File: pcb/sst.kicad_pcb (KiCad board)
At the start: 2 copper layers, 80 x 85 mm, 36 parts, among them X1 CONN_INPUTS, X2 CONN_PWR, X3 CONN_SPI, X4 CONN_I2C, X5 CONN_INPUTS

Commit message: [2024-12-24 15:48] coursework for this day
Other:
- board size 80 x 85 mm -> 80 x 84.8 mm
- board text added: "0"
- board text added: "0 mm"
- board text added: "0,0000 mm / 0,0000 mm"
- board text added: "0,01 mm"
- board text added: "0,02"
- board text added: "0,035 mm"
- board text added: "0,3000 mm"
- board text added: "1"
- board text added: "1,51 mm"
- board text added: "1,6000 mm"
- board text added: "2"
- board text added: "3,3"
- board text added: "4,5"
- board text added: "80,0000 mm x 84,7500 mm"
- board text added: "B.Cu"
- board text added: "B.Mask"
- board text added: "B.Paste"
- board text added: "B.Silkscreen"
- board text added: "Bottom Silk Screen"
- board text added: "Bottom Solder Mask"
- board text added: "Bottom Solder Paste"
- board text added: "F.Cu"
- board text added: "F.Mask"
- board text added: "F.Paste"
- board text added: "F.Silkscreen"
- board text added: "FR4"
- board text added: "None"
- board text added: "Not specified"
- board text added: "Top Silk Screen"
- board text added: "Top Solder Mask"
- board text added: "Top Solder Paste"
- board text added: "copper"
- board text added: "core"
- board text added: "Габариты платы:"
- board text added: "Диэлектрик"
- board text added: "Имя слоя"
- board text added: "Количество слоёв меди:"
- board text added: "Контроль импеданса:"
- board text added: "Краевой соединитель:"
- board text added: "Материал"
- board text added: "Метал. торцы:"
- board text added: "Мин. дорожка/зазор:"
- board text added: "Мин. сверло:"
- board text added: "Нет"
- board text added: "Отн.диэл.прон."
- board text added: "Периферийные полу-отверстия:"
- board text added: "Покрытие меди:"
- board text added: "Танг.угла диэл.потерь"
- board text added: "Тип"
- board text added: "Толщина (мм)"
- board text added: "Толщина платы:"
- board text added: "ХАРАКТЕРИСТИКИ ПЛАТЫ"
- board text added: "Цвет"

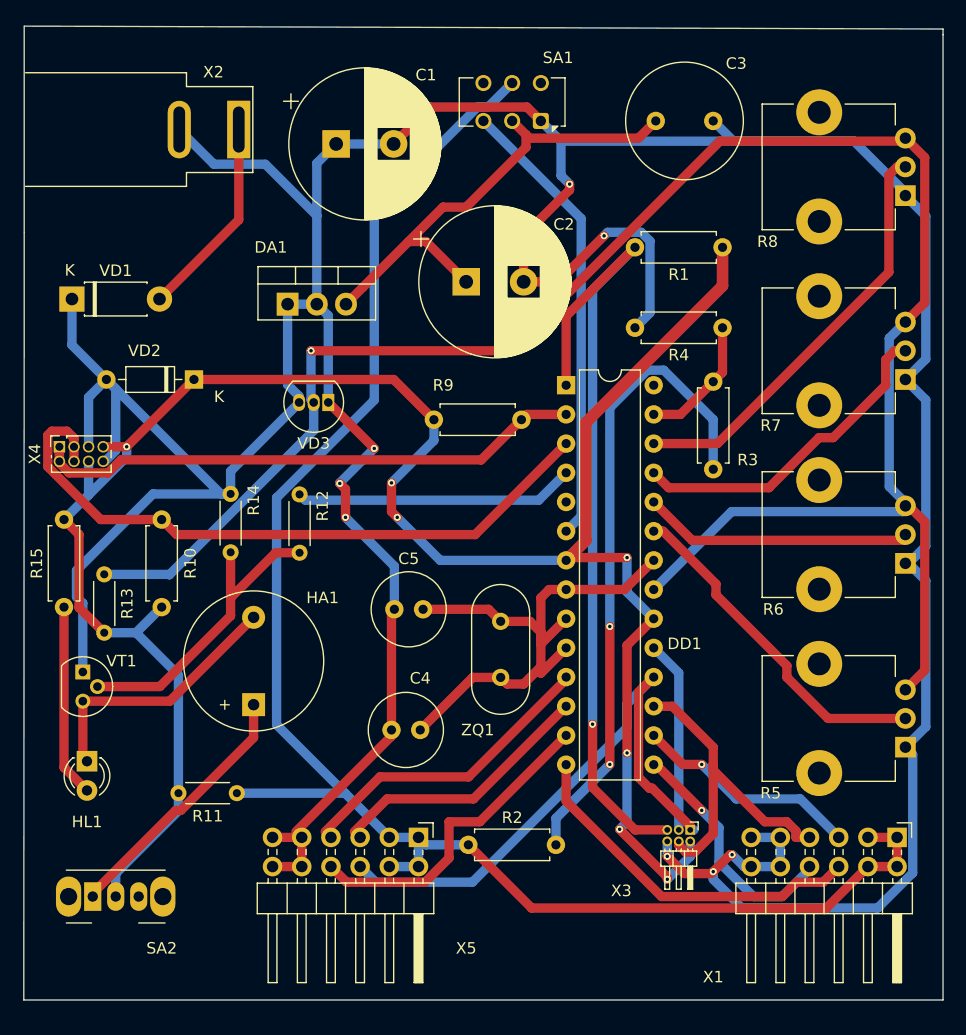
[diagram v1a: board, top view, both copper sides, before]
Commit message: перешёл на девятую версию KiCAD
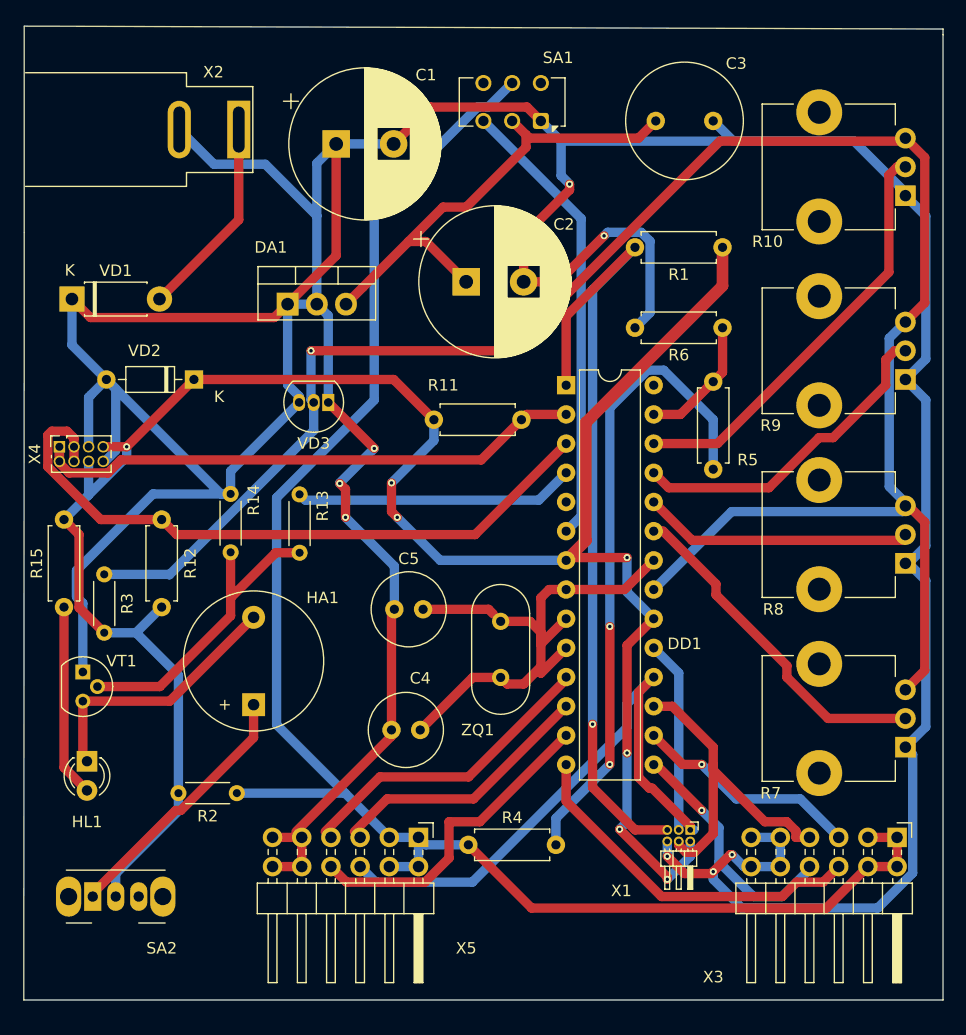
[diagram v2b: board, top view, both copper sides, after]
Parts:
- C2: value 10мк -> 10мк 16В
- DD1: value ATmega328P-P -> Микроконтроллер ATmega328P
- R1: value 10к -> 10к 0,25Вт
- R10: renamed from R8; value 10к -> потенциометр 10к 0,25Вт
- R11: renamed from R9; value 10к -> 10к 0,25Вт
- R12: renamed from R10; value 10к -> 10к 0,25Вт
- R13: renamed from R12; value 22 -> резистор 22 0,25Вт
- R15: value 1к -> 1к 0,25Вт
- R2: renamed from R11; value 22 -> 22 0,25Вт
- R3: renamed from R13; value 1к -> 1к 0,25Вт
- R4: renamed from R2; value 10к -> 10к 0,25Вт
- R5: renamed from R3; value 10к -> 10к 0,25Вт
- R6: renamed from R4; value 10к -> 10к 0,25Вт
- R7: renamed from R5; value 10к -> 10к 0,25Вт
- R8: renamed from R6; value 10к -> потенциометр 10к 0,25Вт
- R9: renamed from R7; value 10к -> потенциометр 10к 0,25Вт
- renumbered X3 to X1, X1 to X3
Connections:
- net Vbat renamed U_{bat}
- C1 pad 1: GND -> Net-(DA1-VI)
- C4 pad 1: /<NO NET> -> Net-(DD1-XTAL1/PB6)
- C5 pad 2: /<NO NET> -> Net-(DD1-XTAL2/PB7)
- DA1 pad 1: GND -> Net-(DA1-VI)
- DD1 pad 10: /<NO NET> -> Net-(DD1-XTAL2/PB7)
- DD1 pad 22: /<NO NET> -> Net-(DD1-XTAL2/PB7)
- DD1 pad 8: /<NO NET> -> Net-(DD1-XTAL1/PB6)
- DD1 pad 9: /<NO NET> -> Net-(DD1-XTAL1/PB6)
- VD1 pad 1: GND -> Net-(DA1-VI)
- VD3 pad 1: GND -> (no net)
- VD3 pad 2: +2V5 -> (no net)
- VD3 pad 3: GND -> (no net)
- ZQ1 pad 1: /<NO NET> -> Net-(DD1-XTAL2/PB7)
- ZQ1 pad 2: /<NO NET> -> Net-(DD1-XTAL1/PB6)
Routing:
- net /<NO NET>: track 49.3 -> 0.00 mm
- net (no net): track 0.00 -> 42.1 mm
- net Net-(DA1-VI): track 0.00 -> 35.6 mm
- net Net-(DD1-XTAL2/PB7): track 0.00 -> 6.27 mm

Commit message: трассировка: два слоя, но без переходных отверстий
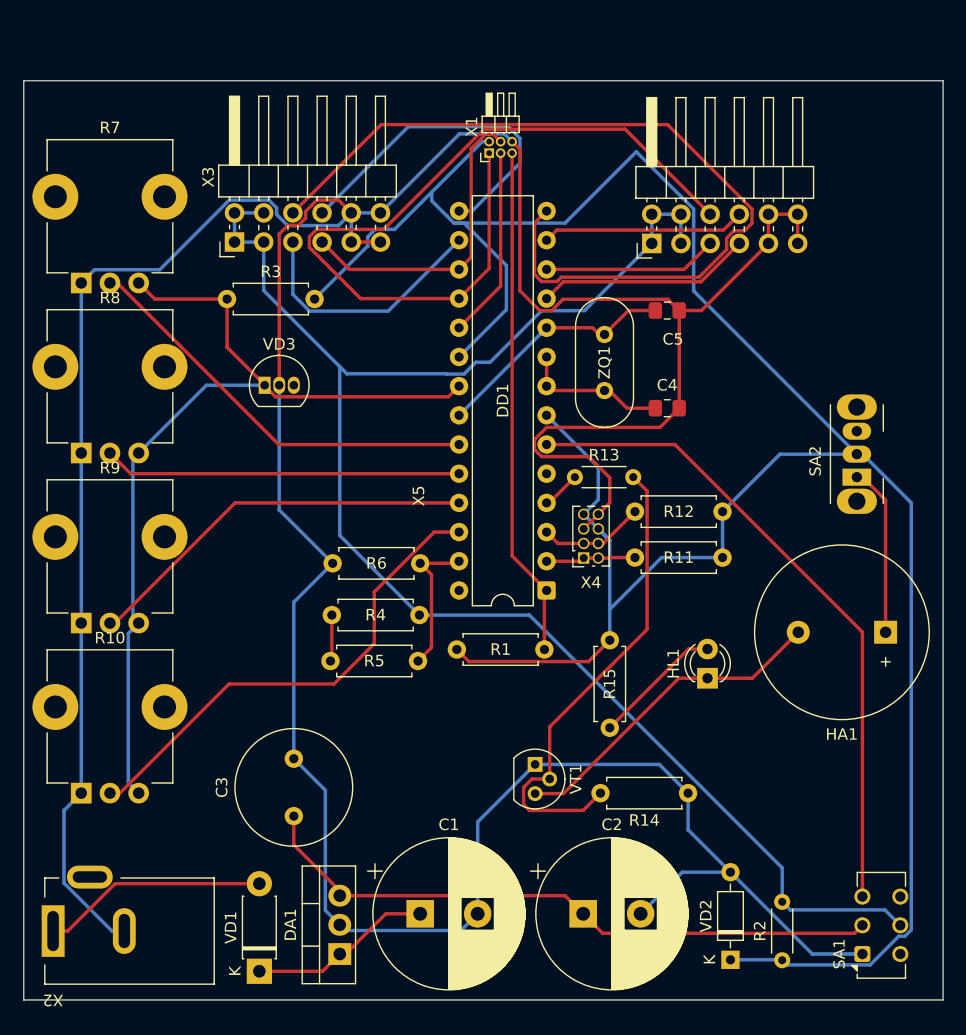
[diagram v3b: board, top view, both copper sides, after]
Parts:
- C4, C5: footprint Capacitor_THT:C_Radial_D6.3mm_H7.0mm_P2.50mm -> Capacitor_SMD:C_0805_2012Metric_Pad1.18x1.45mm_HandSolder
- DD1: value Микроконтроллер ATmega328P -> ATmega328P-P
- HA1: footprint Buzzer_Beeper:Buzzer_12x9.5RM7.6 -> Buzzer_Beeper:Buzzer_15x7.5RM7.6
- R13: value резистор 22 0,25Вт -> 22 0,25Вт
- R14: value 10к -> 10к 0,25Вт; footprint Resistor_THT:R_Axial_DIN0204_L3.6mm_D1.6mm_P5.08mm_Horizontal -> Resistor_THT:R_Axial_DIN0207_L6.3mm_D2.5mm_P7.62mm_Horizontal
- R3: footprint Resistor_THT:R_Axial_DIN0204_L3.6mm_D1.6mm_P5.08mm_Horizontal -> Resistor_THT:R_Axial_DIN0207_L6.3mm_D2.5mm_P7.62mm_Horizontal
- R7: value 10к 0,25Вт -> потенциометр 10к 0,25Вт
- VD1: value VD_Schottky -> 1N5817 шотки
- VD2: value VD_Schottky -> 5,1В шотки
- X2: footprint Connector_BarrelJack:BarrelJack_SwitchcraftConxall_RAPC10U_Horizontal -> Connector_BarrelJack:BarrelJack_Kycon_KLDX-0202-xC_Horizontal
- moved R10 88.6 mm to (124.8, 157.2), turned to 0 degrees
- moved R7 82.3 mm to (124.8, 112.8), turned to 0 degrees
- moved SA1 77.7 mm to (192.7, 171.2), turned to 90 degrees
- moved X3 77.5 mm to (138.1, 109.2), turned to 90 degrees
- moved SA2 75.9 mm to (192.3, 129.7), turned to 90 degrees
- moved R9 74.8 mm to (124.8, 142.4), turned to 0 degrees
- moved R8 72.4 mm to (124.8, 127.6), turned to 0 degrees
- moved X2 71.6 mm to (122.3, 169.2), turned to 180 degrees
- moved VD2 68.8 mm to (181.3, 171.7), turned to 90 degrees
- moved C3 68.2 mm to (143.3, 159.2), turned to 90 degrees
- moved C1 67.4 mm to (154.3, 167.7)
- moved X1 61.4 mm to (160.3, 101.5), turned to 90 degrees
- moved VD1 60.7 mm to (140.3, 172.7), turned to 90 degrees
- moved DA1 56.7 mm to (147.3, 171.2), turned to 90 degrees
- moved C2 55.9 mm to (168.4, 167.7)
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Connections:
- DD1 pad 21: +2V5 -> +2,5V
- R10 pad 3: +2V5 -> +2,5V
- R3 pad 1: +2V5 -> +2,5V
- R7 pad 3: +2V5 -> +2,5V
- R8 pad 3: +2V5 -> +2,5V
- R9 pad 3: +2V5 -> +2,5V
- VD3 pad 1: (no net) -> +2,5V
- VD3 pad 2: (no net) -> GND
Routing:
- net +2V5: track 167.1 -> 0.00 mm, vias 1 -> 0
- net +2,5V: track 0.00 -> 79.0 mm
- net Net-(R4-Pad2): track 56.6 -> 4.05 mm, vias 2 -> 0
- net /SCL: track 58.3 -> 9.25 mm
- net Net-(DD1-PB0): track 31.4 -> 75.2 mm
- net (no net): track 42.1 -> 0.00 mm
- net /SDA: track 49.3 -> 7.82 mm
- net GND: track 381.2 -> 340.5 mm, vias 8 -> 0
- net +5V: track 188.9 -> 222.4 mm, vias 7 -> 0
- net Net-(DD1-~{RESET}/PC6): track 71.0 -> 44.5 mm, vias 1 -> 0
- net Net-(DD1-PD2): track 24.4 -> 3.39 mm
- net Net-(DD1-PB4): track 50.9 -> 71.3 mm
- net Net-(DA1-VI): track 35.6 -> 16.1 mm
- net Net-(DD1-PD4): track 39.8 -> 57.3 mm
- net Net-(DD1-XTAL2/PB7): track 6.27 -> 21.3 mm
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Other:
- board size 80 x 84.8 mm -> 80 x 80 mm
- board text removed: "0"
- board text removed: "0 mm"
- board text removed: "0,0000 mm / 0,0000 mm"
- board text removed: "0,01 mm"
- board text removed: "0,02"
- board text removed: "0,035 mm"
- board text removed: "0,3000 mm"
- board text removed: "1"
- board text removed: "1,51 mm"
- board text removed: "1,6000 mm"
- board text removed: "2"
- board text removed: "3,3"
- board text removed: "4,5"
- board text removed: "80,0000 mm x 84,7500 mm"
- board text removed: "B.Cu"
- board text removed: "B.Mask"
- board text removed: "B.Paste"
- board text removed: "B.Silkscreen"
- board text removed: "Bottom Silk Screen"
- board text removed: "Bottom Solder Mask"
- board text removed: "Bottom Solder Paste"
- board text removed: "F.Cu"
- board text removed: "F.Mask"
- board text removed: "F.Paste"
- board text removed: "F.Silkscreen"
- board text removed: "FR4"
- board text removed: "None"
- board text removed: "Not specified"
- board text removed: "Top Silk Screen"
- board text removed: "Top Solder Mask"
- board text removed: "Top Solder Paste"
- board text removed: "copper"
- board text removed: "core"
- board text removed: "Габариты платы:"
- board text removed: "Диэлектрик"
- board text removed: "Имя слоя"
- board text removed: "Количество слоёв меди:"
- board text removed: "Контроль импеданса:"
- board text removed: "Краевой соединитель:"
- board text removed: "Материал"
- board text removed: "Метал. торцы:"
- board text removed: "Мин. дорожка/зазор:"
- board text removed: "Мин. сверло:"
- board text removed: "Нет"
- board text removed: "Отн.диэл.прон."
- board text removed: "Периферийные полу-отверстия:"
- board text removed: "Покрытие меди:"
- board text removed: "Танг.угла диэл.потерь"
- board text removed: "Тип"
- board text removed: "Толщина (мм)"
- board text removed: "Толщина платы:"
- board text removed: "ХАРАКТЕРИСТИКИ ПЛАТЫ"
- board text removed: "Цвет"
